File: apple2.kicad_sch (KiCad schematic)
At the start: 0 parts

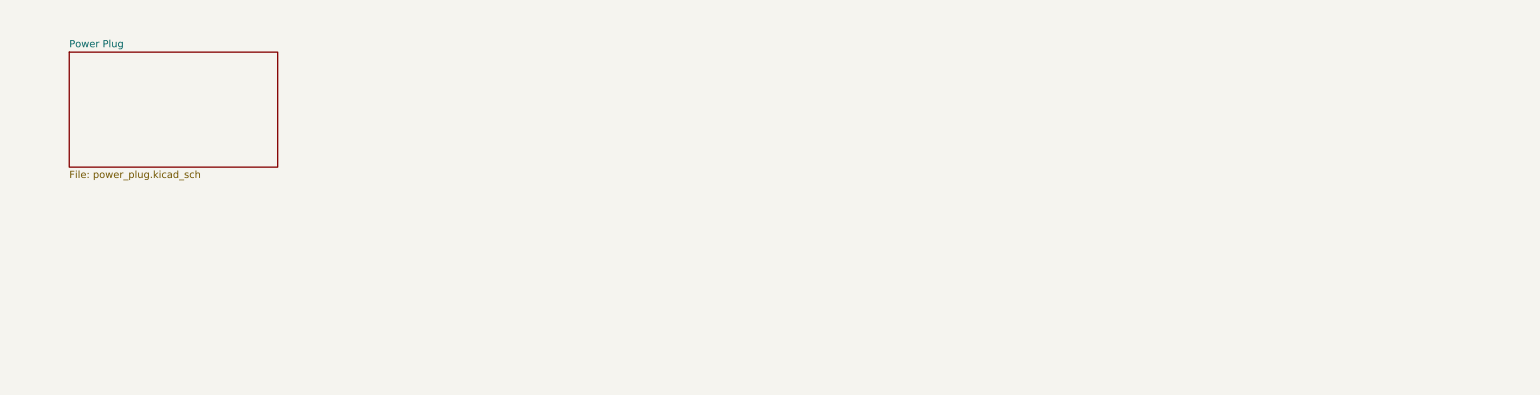
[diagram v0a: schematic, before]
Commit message: Add video output section
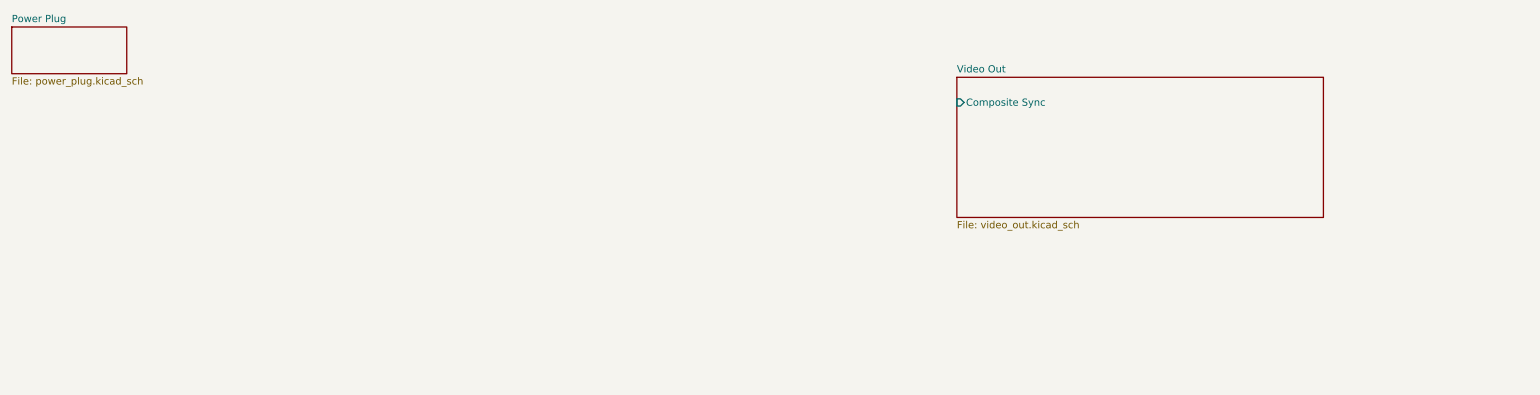
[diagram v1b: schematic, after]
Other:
- added sheet Video Out (video_out.kicad_sch)
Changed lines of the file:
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@@
     (comment 1 "Main Logic Board B20-0044 Rev 01")
   )
-  (sheet (at 24.13 20.32) (size 36.83 20.32) (fields_autoplaced)
+  (sheet (at 13.97 15.875) (size 20.32 8.255) (fields_autoplaced)
     (stroke (width 0.1524) (type solid))
     (fill (color 0 0 0 0.0000))
-    (property "Sheetname" "Power Plug" (at 24.13 19.6084 0) (show_name)
+    (property "Sheetname" "Power Plug" (at 13.97 15.1634 0) (show_name)
       (effects (font (size 1.27 1.27)) (justify left bottom))
     )
-    (property "Sheetfile" "power_plug.kicad_sch" (at 24.13 41.2246 0)
+    (property "Sheetfile" "power_plug.kicad_sch" (at 13.97 24.7146 0)
       (effects (font (size 1.27 1.27)) (justify left top))
     )
@@
       )
     )
+  )
+  (sheet (at 180.975 24.765) (size 64.77 24.765) (fields_autoplaced)
+    (stroke (width 0.1524) (type solid))
+    (fill (color 0 0 0 0.0000))
+    (property "Sheetname" "Video Out" (at 180.975 24.0534 0) (show_name)
+      (effects (font (size 1.27 1.27)) (justify left bottom))
+    )
+    (property "Sheetfile" "video_out.kicad_sch" (at 180.975 50.1146 0)
+      (effects (font (size 1.27 1.27)) (justify left top))
+    )
+    (pin "Composite Sync" input (at 180.975 29.21 180)
+      (effects (font (size 1.27 1.27)) (justify left))
+    )
+    (instances
+      (project "apple2"
+        (path "/7d36cf7e-8de7-4392-bd63-1a9c9576ca74" (page "3"))
+      )
+    )

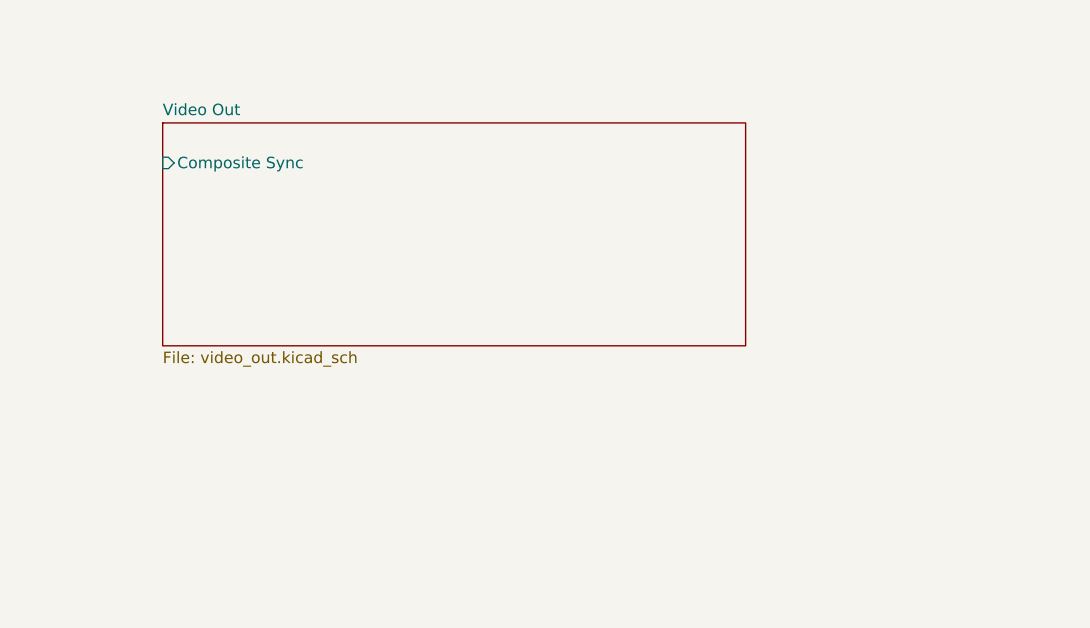
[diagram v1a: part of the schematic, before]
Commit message: Add Reset Circuit
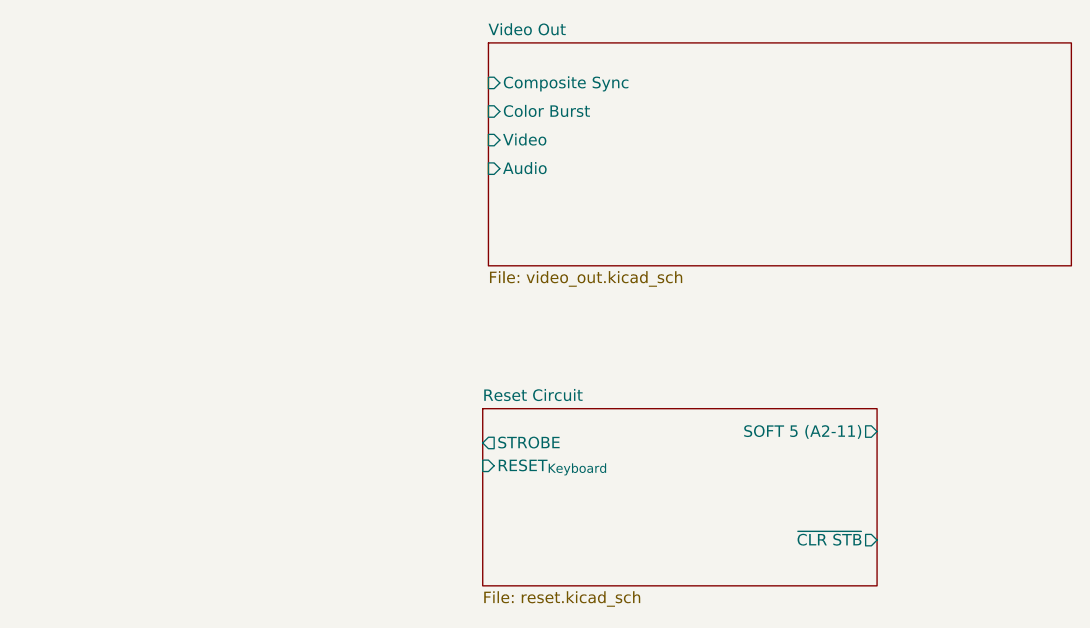
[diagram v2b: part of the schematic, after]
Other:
- added sheet Reset Circuit (reset.kicad_sch)
- sheet Video Out ports: added Audio, Color Burst, Video; removed none
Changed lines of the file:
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@@
     )
   )
-  (sheet (at 180.975 24.765) (size 64.77 24.765) (fields_autoplaced)
+  (sheet (at 216.535 56.515) (size 43.815 19.685) (fields_autoplaced)
     (stroke (width 0.1524) (type solid))
     (fill (color 0 0 0 0.0000))
-    (property "Sheetname" "Video Out" (at 180.975 24.0534 0) (show_name)
+    (property "Sheetname" "Reset Circuit" (at 216.535 55.8034 0) (show_name)
       (effects (font (size 1.27 1.27)) (justify left bottom))
     )
-    (property "Sheetfile" "video_out.kicad_sch" (at 180.975 50.1146 0)
+    (property "Sheetfile" "reset.kicad_sch" (at 216.535 76.7846 0)
       (effects (font (size 1.27 1.27)) (justify left top))
     )
-    (pin "Composite Sync" input (at 180.975 29.21 180)
+    (pin "STROBE" output (at 216.535 60.325 180)
       (effects (font (size 1.27 1.27)) (justify left))
     )
+    (pin "SOFT 5 (A2-11)" output (at 260.35 59.055 0)
+      (effects (font (size 1.27 1.27)) (justify right))
+    )
+    (pin "RESET_{Keyboard}" input (at 216.535 62.865 180)
+      (effects (font (size 1.27 1.27)) (justify left))
+    )
+    (pin "~{CLR STB}" output (at 260.35 71.12 0)
+      (effects (font (size 1.27 1.27)) (justify right))
+    )
+    (instances
+      (project "apple2"
+        (path "/7d36cf7e-8de7-4392-bd63-1a9c9576ca74" (page "4"))
+      )
+    )
+  )
+  (sheet (at 217.17 15.875) (size 64.77 24.765) (fields_autoplaced)
+    (stroke (width 0.1524) (type solid))
+    (fill (color 0 0 0 0.0000))
+    (property "Sheetname" "Video Out" (at 217.17 15.1634 0) (show_name)
+      (effects (font (size 1.27 1.27)) (justify left bottom))
+    )
+    (property "Sheetfile" "video_out.kicad_sch" (at 217.17 41.2246 0)
+      (effects (font (size 1.27 1.27)) (justify left top))
+    )
+    (pin "Composite Sync" input (at 217.17 20.32 180)
+      (effects (font (size 1.27 1.27)) (justify left))
+    )
+    (pin "Color Burst" input (at 217.17 23.495 180)
+      (effects (font (size 1.27 1.27)) (justify left))
+    )
+    (pin "Video" input (at 217.17 26.67 180)
+      (effects (font (size 1.27 1.27)) (justify left))
+    )
+    (pin "Audio" input (at 217.17 29.845 180)
+      (effects (font (size 1.27 1.27)) (justify left))
+    )
